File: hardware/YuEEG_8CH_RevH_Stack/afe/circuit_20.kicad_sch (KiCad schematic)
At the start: 6 parts, among them U403 TPS73225DBVR

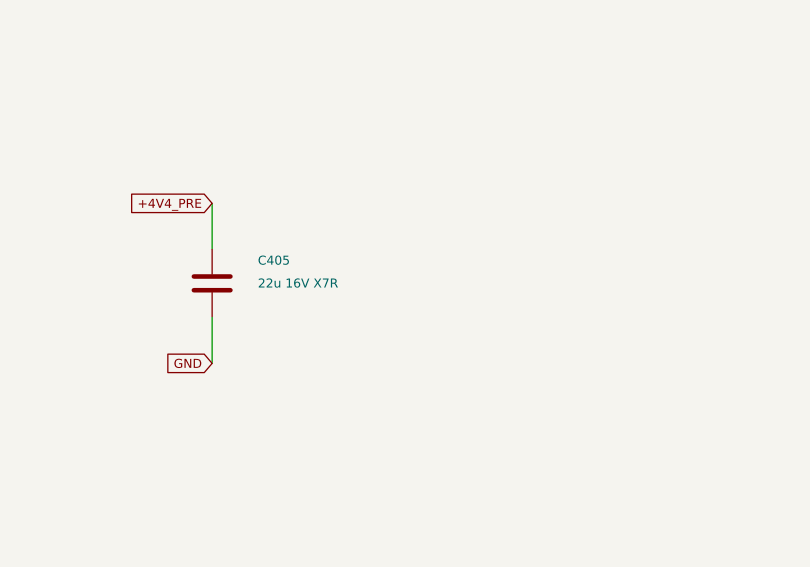
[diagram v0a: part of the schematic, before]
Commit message: Refine stacked AFE clearance and rounded USB mouth geometry
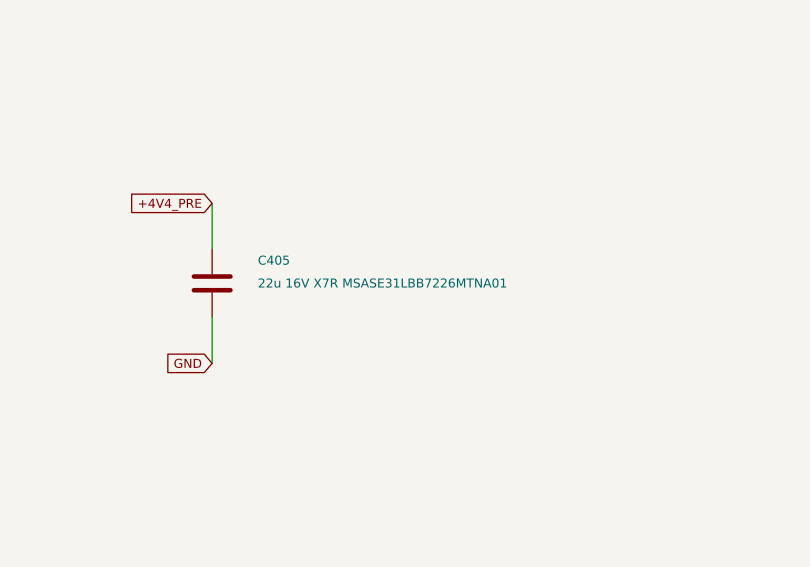
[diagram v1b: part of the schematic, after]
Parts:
- C405: value 22u 16V X7R -> 22u 16V X7R MSASE31LBB7226MTNA01; footprint Capacitor_SMD:C_1206_3216Metric -> YuEEG:TY_MSASE31LBB7226MTNA01_1206
